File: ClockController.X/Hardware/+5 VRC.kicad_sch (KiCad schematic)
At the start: 4 parts, among them U2 AS78L05RTR-E1

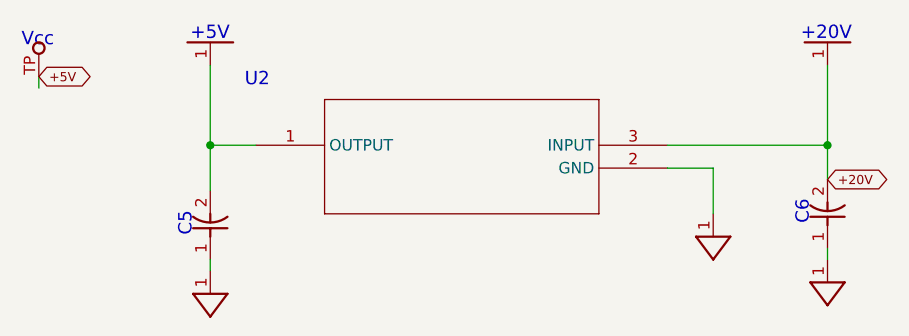
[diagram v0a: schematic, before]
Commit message: Replace the imported objects with native kicad equivalents
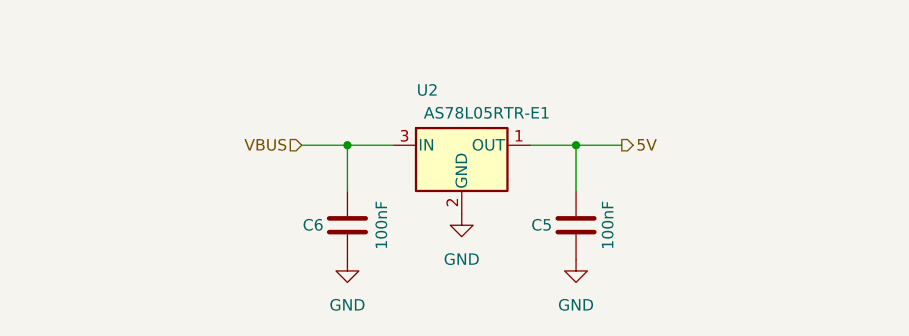
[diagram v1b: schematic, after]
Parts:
- removed Vcc0: Most Density, Clock Controller:TP_1.25MM, symbol Clock Controller-eagle-import:TP_1.25MM
- C5, C6: symbol Clock Controller-eagle-import:CAP_0805 -> Device:C
- U2: symbol Clock Controller-eagle-import:AS78L05RTR-E1 -> Regulator_Linear:L78L05_SOT89
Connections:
- net +20V_35 renamed VBUS
- net +5V renamed 5V
- net GND_DIGITAL renamed GND
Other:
- note removed: "+20V"
- note removed: "+5V"
- note removed: "C5"
- note removed: "C6"
- note removed: "U2"
- note removed: "Vcc"
